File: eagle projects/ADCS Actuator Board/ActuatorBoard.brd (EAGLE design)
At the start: 91 x 91 mm, 256 parts, among them J4 OSTVN08A150, J5 OSTVN08A150, J6 OSTVN08A150, U10 TVS991, U11 BD621F-E2, U12 ADS7841E_2K5, U13 ADS7841E_2K5, U15 TLV9051IDCKR, U16 BD621F-E2, U17 DRV10970_MOTOR_DRIVERDRV10970, U18 DRV10970_MOTOR_DRIVERDRV10970, U19 TLV9051IDCKR, U20 DRV10970_MOTOR_DRIVERDRV10970, U21 TLV9051IDCKR, U22 BD621F-E2, U23 TLV9051IDCKR, U24 TLV9051IDCKR, U25 ADS7841E_2K5, U26 TLV9051IDCKR, U27 ADS7841E_2K5, U28 TLV9051IDCKR, U29 TLV9051IDCKR, U30 TLV9051IDCKR, U31 TLV9051IDCKR, U32 TLV9051IDCKR, U4 ADS7841E_2K5, U6 TLV9051IDCKR, U7 TVS991, U8 TVS991, U9 ADS7841E_2K5

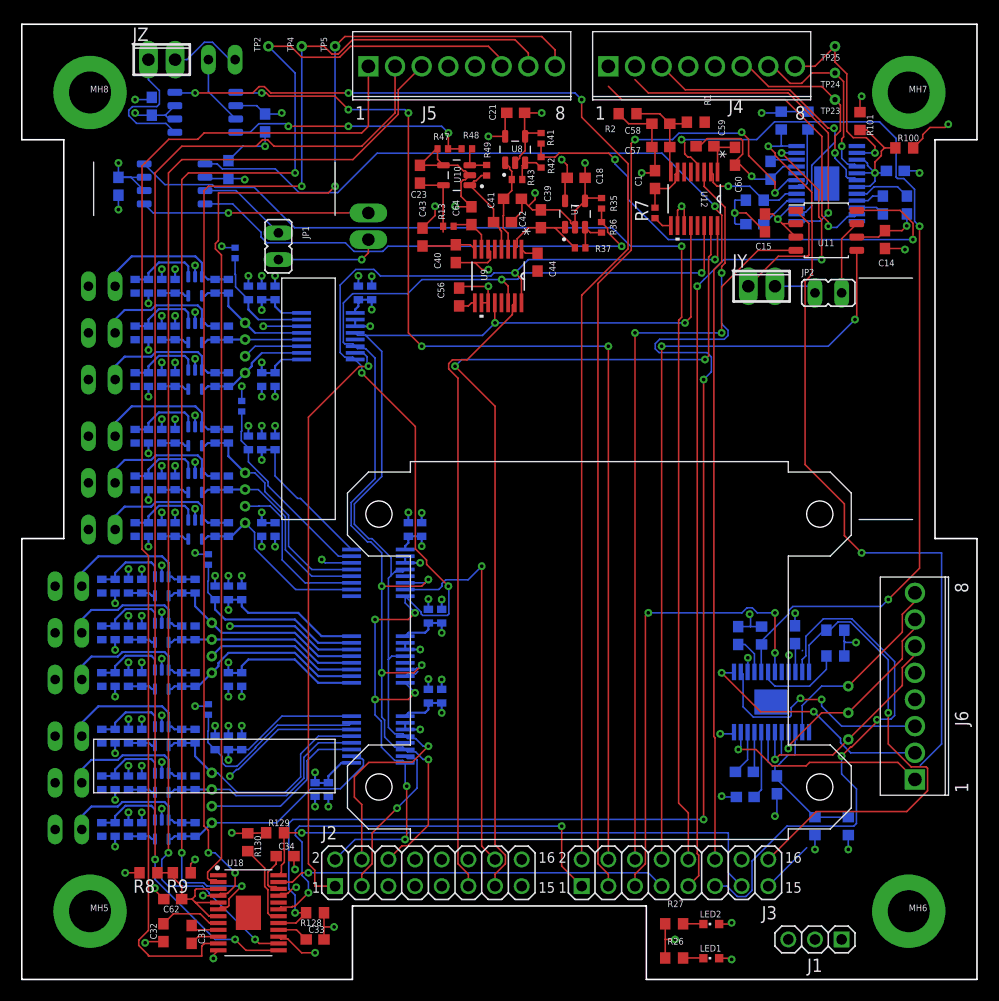
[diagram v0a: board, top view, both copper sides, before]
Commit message: replaced 10u caps with 4.7u
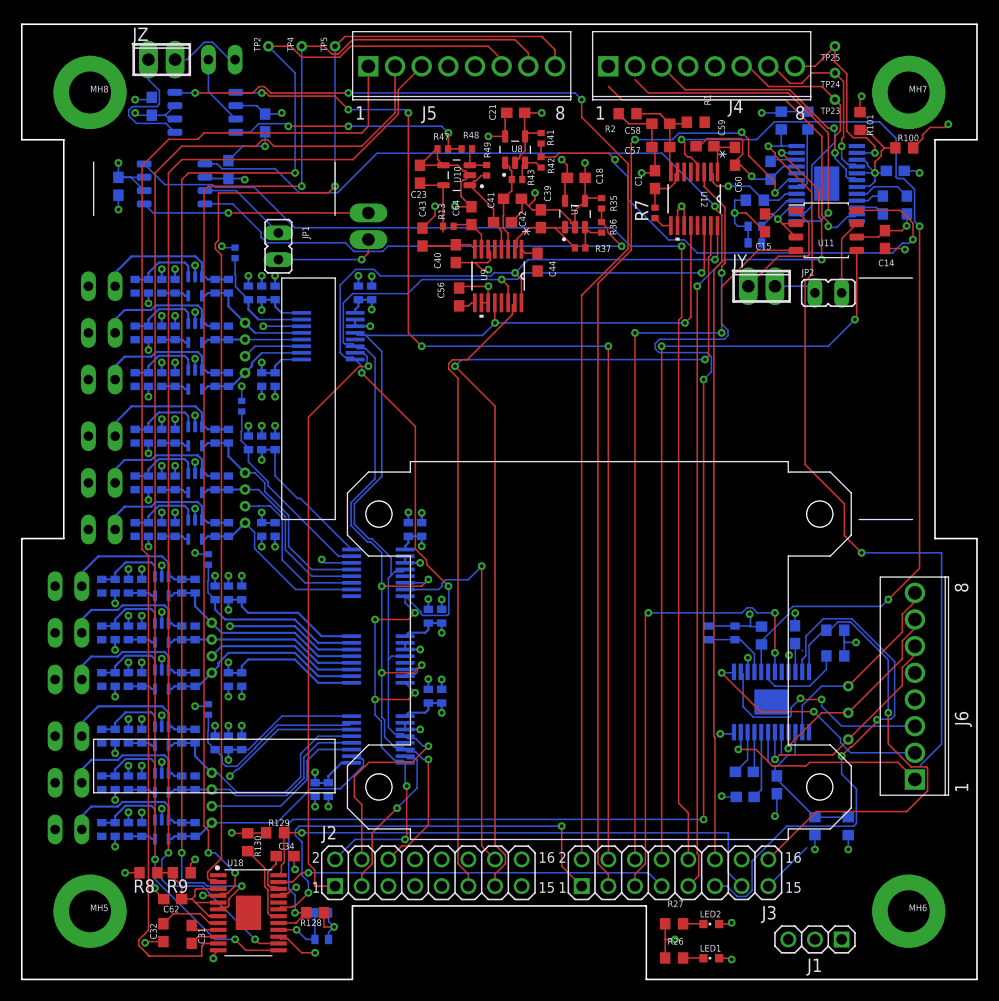
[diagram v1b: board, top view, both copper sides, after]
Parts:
- removed C29, C33, C37: 10u, rcl:C0603
- added C2, C3, C4, C5, C6, C7: 4.7u, resistor:C0402
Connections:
- removed net N$28: J2.15
- net +3V3: now also J2.15
- net GND: now also C2.2, C3.2, C4.2, C5.2, C6.2, C7.2; no longer C29.2, C33.2, C37.2
- net N$26: now also C4.1, C5.1; no longer C29.1
- net N$42: now also C6.1, C7.1; no longer C33.1
- net N$53: now also C2.1, C3.1; no longer C37.1
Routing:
- net GND: track 246.7 -> 253.2 mm
- net N$42: track 3.01 -> 6.38 mm, vias 0 -> 1
- net N$53: track 3.64 -> 6.68 mm
- net N$26: track 4.06 -> 5.92 mm
- net MAG_CUR_SEN_Y: track 49.2 -> 50.2 mm
- added copper zone on layer 15, net +3V3

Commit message: laid out polygons for power plane
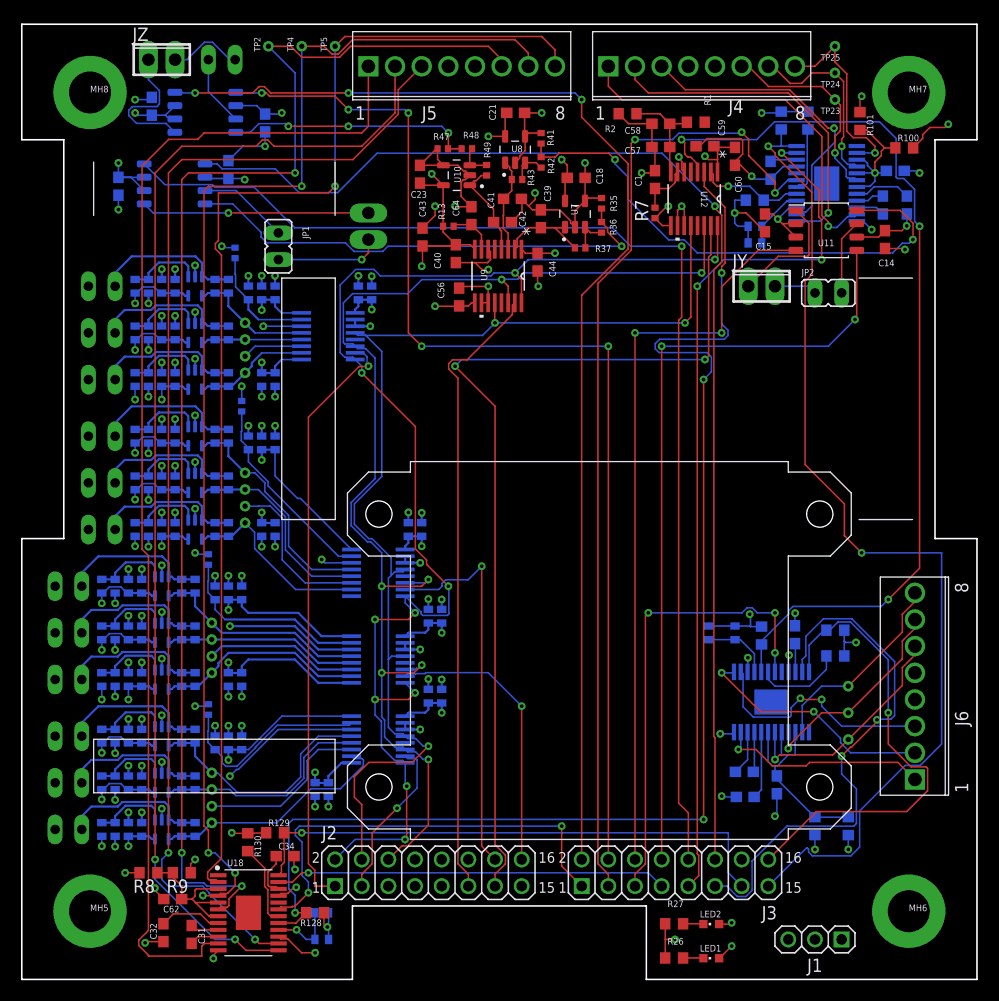
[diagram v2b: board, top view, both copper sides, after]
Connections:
- net !CS!_SUN_X+: now also J2.16
- net !CS!_SUN_X-: no longer J2.16
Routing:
- net +3V3: track 175.4 -> 228.9 mm, vias 22 -> 44
- net !CS!_SUN_X+: track 1.40 -> 27.2 mm, vias 0 -> 1
- net RW_Y_OUTFG: track 81.2 -> 98.0 mm
- net GND: track 253.2 -> 257.8 mm, vias 114 -> 117
- net Y_PHASE_C: track 34.4 -> 36.3 mm
- net Y_PHASE_B: track 31.5 -> 32.8 mm
- net N$63: track 12.9 -> 14.2 mm
- net N$55: track 12.9 -> 14.2 mm
- net N$44: track 12.9 -> 14.2 mm
- net N$33: track 12.9 -> 14.2 mm
- added copper zone on layer 15, net +5V

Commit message: moved ADCs and X reaction wheel driver
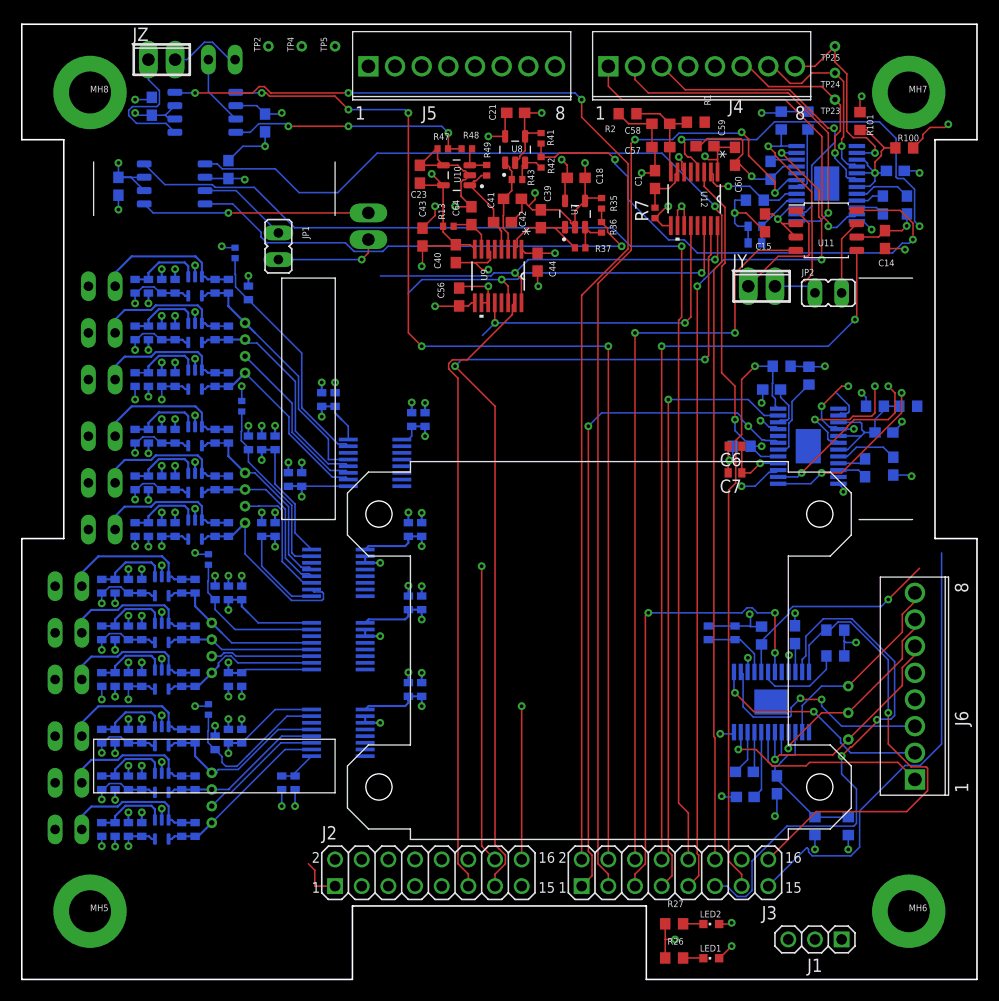
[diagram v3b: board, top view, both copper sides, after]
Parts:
- moved R8 84.9 mm to (84.5, 54.6), flipped to the bottom
- moved C32 82.5 mm to (83.0, 48.9), flipped to the bottom
- moved C62 81.0 mm to (82.1, 52.1), flipped to the bottom
- moved R9 79.6 mm to (81.3, 54.6), flipped to the bottom
- moved C31 78.1 mm to (80.3, 48.7), flipped to the bottom
- moved R130 69.5 mm to (75.0, 57.5), flipped to the bottom
- moved U18 69.4 mm to (74.9, 50.8), flipped to the bottom
- moved R129 65.6 mm to (72.4, 58.4), flipped to the bottom
- moved C34 64.2 mm to (71.4, 56.2), flipped to the bottom
- moved R128 60.2 mm to (68.6, 50.8), flipped to the bottom
- moved C6 59.4 mm to (67.9, 50.8), flipped to the top
- moved C7 59.4 mm to (67.9, 48.3), flipped to the top
- moved C79 13.1 mm to (37.1, 53.3)
- moved C80 13.1 mm to (38.4, 53.3)
- moved U4 12.9 mm to (33.7, 49.2)
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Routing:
- net X_PHASE_C: track 112.8 -> 0.00 mm
- net X_HALL_C: track 124.6 -> 12.0 mm, vias 3 -> 2
- net X_HALL_A: track 115.5 -> 3.62 mm, vias 1 -> 0
- net X_HALL_B: track 118.4 -> 8.04 mm, vias 4 -> 3
- net X_PHASE_B: track 112.0 -> 16.5 mm
- net RW_X_I_SENS: track 127.1 -> 32.3 mm, vias 4 -> 2
- net X_PHASE_A: track 111.0 -> 16.5 mm
- net UCB0_SPI_CLK: track 126.5 -> 39.0 mm, vias 10 -> 2
- net UCB0_SPI_MOSI: track 117.7 -> 35.9 mm, vias 7 -> 2
- net UCB0_SPI_MISO: track 108.5 -> 31.2 mm, vias 3 -> 2
- net !CS!_SUN_Y-: track 56.8 -> 5.06 mm, vias 1 -> 0
- net RW_Y_OUTFG: track 98.0 -> 62.3 mm, vias 2 -> 1
- net GND: track 257.8 -> 224.4 mm, vias 117 -> 112
- net RW_Z_I_SENS: track 89.0 -> 56.4 mm
- net RW_X_SPEED_CTRL: track 42.0 -> 64.3 mm
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- removed copper zone on layer 15, net +3V3
- removed copper zone on layer 15, net +5V

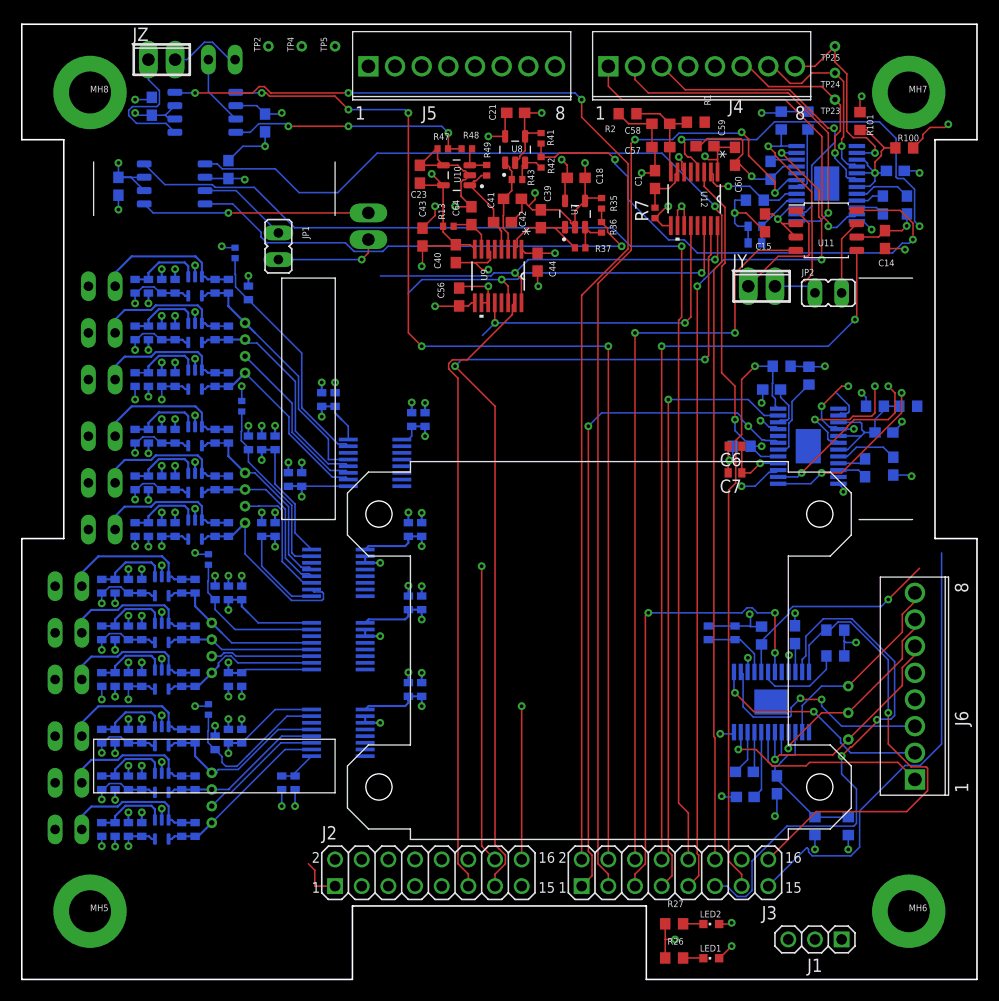
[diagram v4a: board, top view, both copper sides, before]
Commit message: redid traces for new positioning
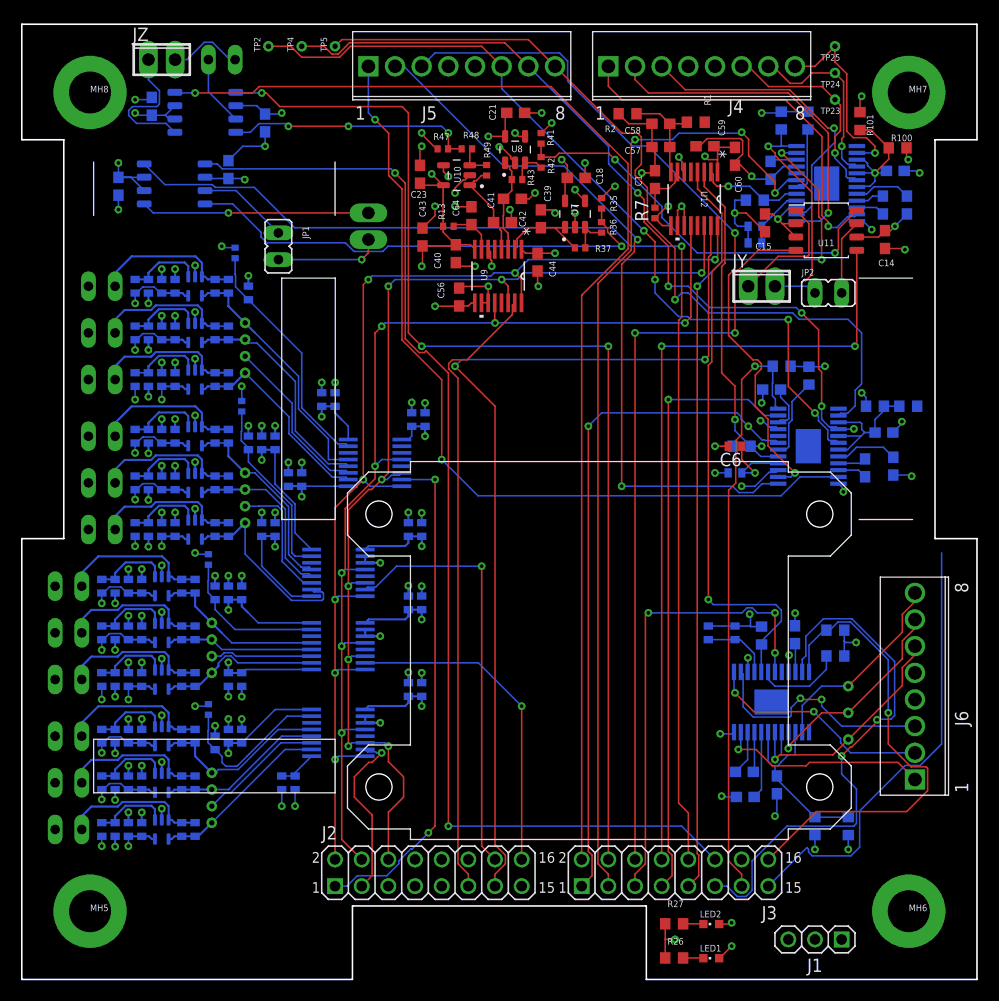
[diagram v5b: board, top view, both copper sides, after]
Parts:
- moved R100 0.64 mm to (83.4, 79.2)
- flipped C7 to the bottom, turned to 0 degrees
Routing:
- net X_PHASE_C: track 0.00 -> 80.3 mm, vias 0 -> 2
- net X_HALL_A: track 3.62 -> 79.4 mm, vias 0 -> 1
- net UCB0_SPI_MISO: track 31.2 -> 103.5 mm, vias 2 -> 7
- net UCB0_SPI_CLK: track 39.0 -> 109.8 mm, vias 2 -> 7
- net X_HALL_B: track 8.04 -> 77.9 mm, vias 3 -> 5
- net UCB0_SPI_MOSI: track 35.9 -> 104.7 mm, vias 2 -> 8
- net X_HALL_C: track 12.0 -> 79.4 mm, vias 2 -> 4
- net X_PHASE_B: track 16.5 -> 69.6 mm
- net X_PHASE_A: track 16.5 -> 66.8 mm
- net !CS!_SUN_Y-: track 5.06 -> 49.0 mm, vias 0 -> 2
- net GND: track 224.4 -> 206.6 mm, vias 112 -> 126
- net !CS!_SUN_Y+: track 0.00 -> 16.8 mm, vias 0 -> 1
- net !CS!_SUN_X+: track 14.6 -> 31.2 mm
- net !CS!_SUN_X-: track 28.5 -> 40.5 mm
- net MAG_CUR_SEN_Y: track 50.2 -> 38.9 mm
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
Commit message: finished power plane
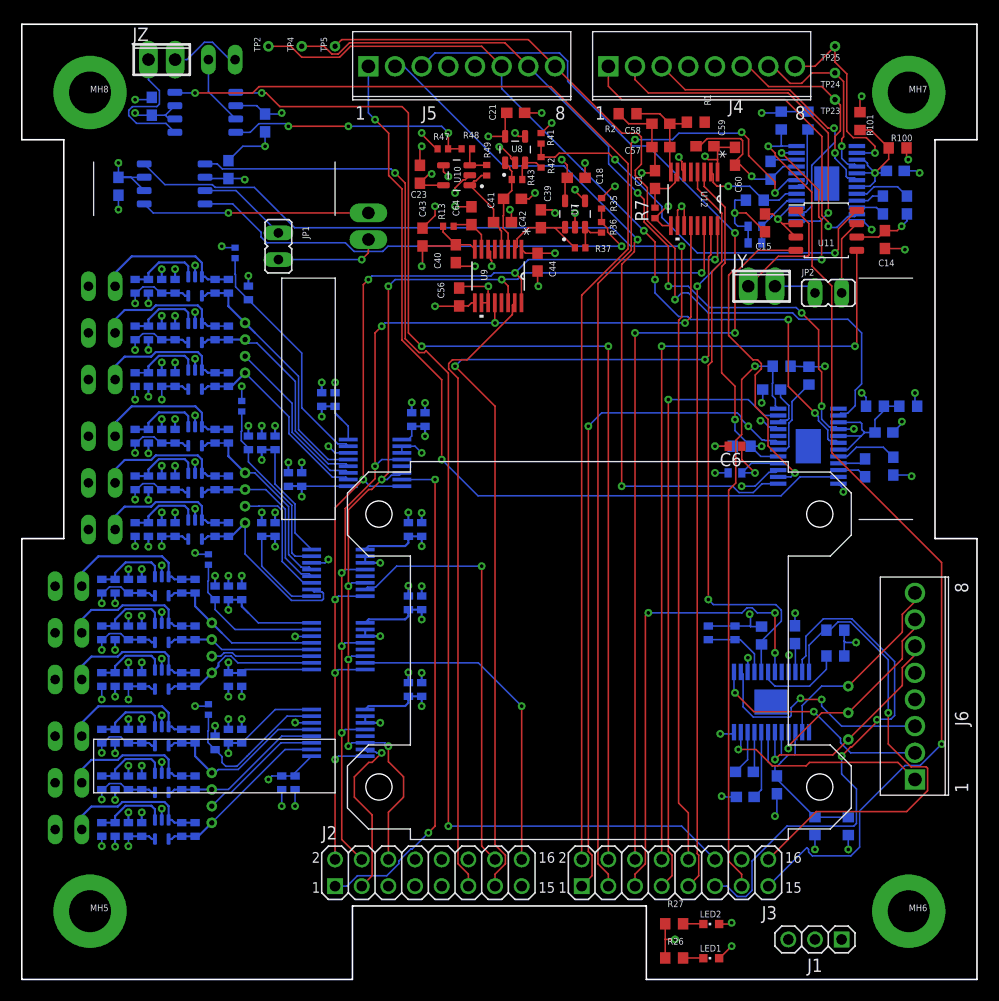
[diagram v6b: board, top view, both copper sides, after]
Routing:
- net RW_Y_OUTFG: track 62.3 -> 93.0 mm, vias 1 -> 2
- net GND: track 206.6 -> 216.4 mm, vias 126 -> 131
- net +3V3: track 229.7 -> 227.1 mm, vias 43 -> 44
- net +5V: track 46.8 -> 48.5 mm, vias 13 -> 14
- net !CS!_SUN_Y-: track 49.0 -> 48.2 mm
- net RW_Z_I_SENS: track 57.0 -> 56.3 mm
- net VINT/2_Y: track 15.0 -> 14.4 mm
- added copper zone on layer 15, net +3V3
- added copper zone on layer 15, net +5V
